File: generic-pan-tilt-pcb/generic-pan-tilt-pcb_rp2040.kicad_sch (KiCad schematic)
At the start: 28 parts, among them U1 RP2040, U2 W25Q32JVSS, Y1 ABM8-272-T3

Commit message: rename again to generic-pan-tilt
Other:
- title: Pan Tilt PCB: RP2040 -> Generic Pan Tilt PCB: RP2040

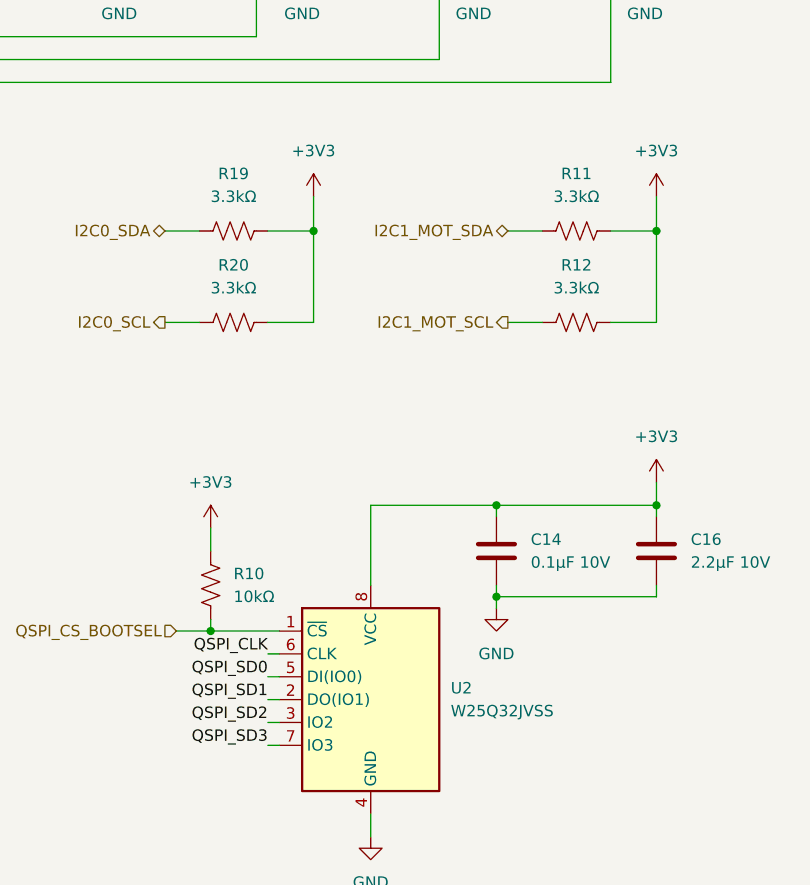
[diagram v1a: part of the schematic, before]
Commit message: pick all footprints, begin layout
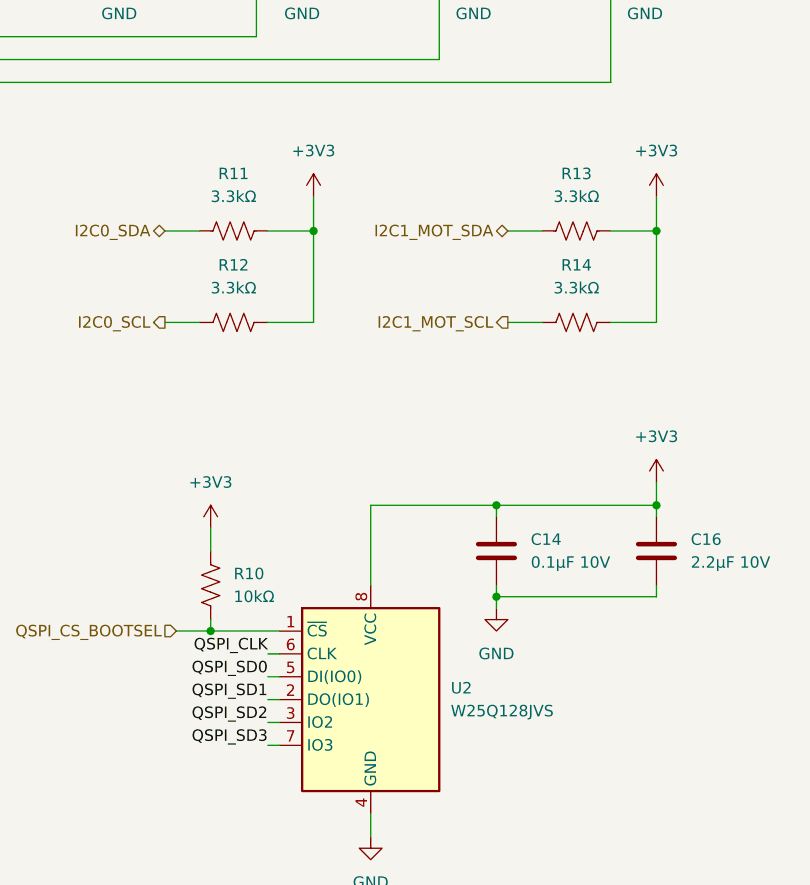
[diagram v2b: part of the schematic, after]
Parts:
- C1, C10, C11, C12, C13, C14, C15, C16, C2, C3, C4, C5, C6, C7, C8, C9: footprint (none) -> Capacitor_SMD:C_0603_1608Metric
- R10, R6, R7, R8, R9: footprint (none) -> Resistor_SMD:R_0603_1608Metric
- R11: renamed from R19; footprint (none) -> Resistor_SMD:R_0603_1608Metric
- R12: renamed from R20; footprint (none) -> Resistor_SMD:R_0603_1608Metric
- R13: renamed from R11; footprint (none) -> Resistor_SMD:R_0603_1608Metric
- R14: renamed from R12; footprint (none) -> Resistor_SMD:R_0603_1608Metric
- U2: value W25Q32JVSS -> W25Q128JVS; symbol Memory_Flash:W25Q32JVSS -> Memory_Flash:W25Q128JVS
- Y1: footprint (none) -> Crystal:Crystal_SMD_3225-4Pin_3.2x2.5mm

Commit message: layout progress
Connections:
- net USB_UNTERMINATED_D+: now reaches R7.2, U1.46 (USB_DM)
- net USB_UNTERMINATED_D-: now reaches R6.2, U1.47 (USB_DP)
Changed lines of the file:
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@@
+		)
+	)
+	(label "USB_UNTERMINATED_D+"
+		(at 43.18 86.36 0)
+		(fields_autoplaced yes)
+		(effects
+			(font
+				(size 1.27 1.27)
+			)
+			(justify left bottom)
 		)
 	)
@@
 		)
 	)
+	(label "USB_UNTERMINATED_D-"
+		(at 43.18 83.82 0)
+		(fields_autoplaced yes)
+		(effects
+			(font
+				(size 1.27 1.27)
+			)
+			(justify left bottom)
+		)
+	)

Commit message: begin new routing
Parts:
- C1, C10, C11, C12, C13, C14, C15, C16, C2, C3, C4, C5, C6, C7, C8, C9: footprint Capacitor_SMD:C_0603_1608Metric -> Capacitor_SMD:C_0402_1005Metric
- R10, R11, R12, R13, R14, R6, R7, R8, R9: footprint Resistor_SMD:R_0603_1608Metric -> Capacitor_SMD:C_0402_1005Metric
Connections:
- net XIN: now reaches C1.2, U1.20 (XIN), Y1.4
- net XOUT: now reaches R9.2, U1.21 (XOUT)
- net XOUT_R: now reaches C2.2, R9.1, Y1.2
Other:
- moved on the sheet: C1, C2, R9, Y1

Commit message: more pcb, kicost maf digikey mouser
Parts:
- U1: digikey# (none) -> 2648-SC0914(13)CT-ND; manf# (none) -> SC0914(13); mouser# (none) -> 358-SC091413
- U2: digikey# (none) -> W25Q128JVSIQCT-ND; manf# (none) -> W25Q128JVSIQ TR; mouser# (none) -> 454-W25Q128JVSIQTR
- Y1: digikey# (none) -> 535-ABM8-272-T3CT-ND; manf# (none) -> ABM8-272-T3; mouser# (none) -> 815-ABM8-272-T3
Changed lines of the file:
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@@
+			)
+		)
+		(property "manf#" "SC0914(13)"
+			(at 93.98 114.3 0)
+			(effects
+				(font
+					(size 1.27 1.27)
+				)
+				(hide yes)
+			)
+		)
+		(property "digikey#" "2648-SC0914(13)CT-ND"
+			(at 93.98 114.3 0)
+			(effects
+				(font
+					(size 1.27 1.27)
+				)
+				(hide yes)
+			)
+		)
+		(property "mouser#" "358-SC091413"
+			(at 93.98 114.3 0)
+			(effects
+				(font
+					(size 1.27 1.27)
+				)
+				(hide yes)
 			)
 		)
@@
 			)
 		)
+		(property "digikey#" "W25Q128JVSIQCT-ND"
+			(at 210.82 125.73 0)
+			(effects
+				(font
+					(size 1.27 1.27)
+				)
+				(hide yes)
+			)
+		)
+		(property "manf#" "W25Q128JVSIQ TR"
+			(at 210.82 125.73 0)
+			(effects
+				(font
+					(size 1.27 1.27)
+				)
+				(hide yes)
+			)
+		)
+		(property "mouser#" "454-W25Q128JVSIQTR"
+			(at 210.82 125.73 0)
+			(effects
+				(font
+					(size 1.27 1.27)
+				)
+				(hide yes)
+			)
+		)
 		(pin "8"
 		)
@@
 			(at 41.91 127 0)
 			(effects
+				(font
+					(size 1.27 1.27)
+				)
+				(hide yes)
+			)
+		)
+		(property "digikey#" "535-ABM8-272-T3CT-ND"
+			(at 41.91 127 0)
+			(effects
+				(font
+					(size 1.27 1.27)
+				)
+				(hide yes)
+			)
+		)
+		(property "manf#" "ABM8-272-T3"
+			(at 41.91 127 0)
+			(effects
+				(font
+					(size 1.27 1.27)
+				)
+				(hide yes)
+			)
+		)
+		(property "mouser#" "815-ABM8-272-T3"
+			(at 41.91 127 0)
+			(effects

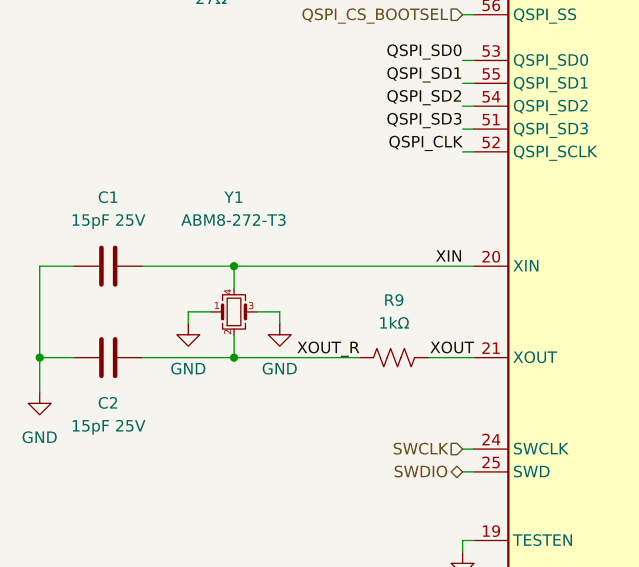
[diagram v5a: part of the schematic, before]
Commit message: transplant hardware guide rp2040
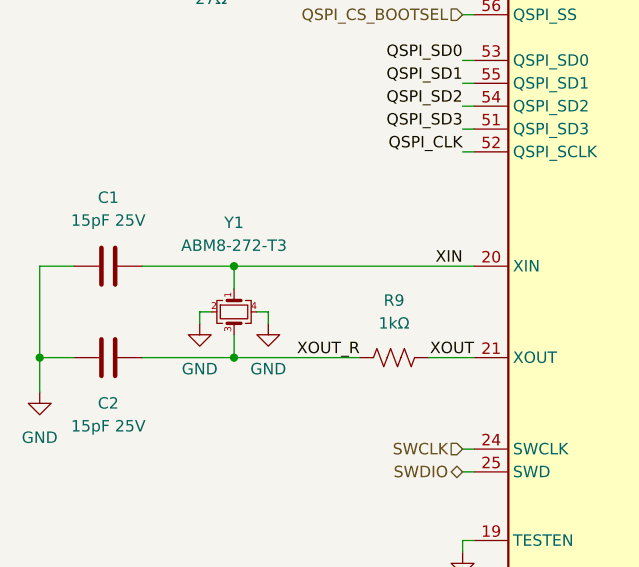
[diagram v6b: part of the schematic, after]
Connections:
- net GND: now also Y1.2, Y1.4; no longer Y1.1, Y1.3
- net XIN: now also Y1.1; no longer Y1.4
- net XOUT_R: now also Y1.3; no longer Y1.2
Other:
- moved on the sheet: Y1
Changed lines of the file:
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@@
 	(wire
 		(pts
-			(xy 36.83 127) (xy 39.37 127)
+			(xy 38.1 127) (xy 39.37 127)
 		)
 		(stroke
@@
 	(wire
 		(pts
+			(xy 44.45 127) (xy 45.72 127)
+		)
+		(stroke
+			(width 0)
+			(type default)
+		)
+	)
+	(wire
+		(pts
 			(xy 226.06 83.82) (xy 229.87 83.82)
 		)
@@
 	(wire
 		(pts
-			(xy 46.99 128.27) (xy 46.99 127)
+			(xy 45.72 128.27) (xy 45.72 127)
 		)
 		(stroke
@@
 	(wire
 		(pts
-			(xy 36.83 128.27) (xy 36.83 127)
+			(xy 38.1 128.27) (xy 38.1 127)
 		)
 		(stroke
@@
 		)
 	)
-	(wire
-		(pts
-			(xy 44.45 127) (xy 46.99 127)
-		)
-		(stroke
-			(width 0)
-			(type default)
-		)
-	)
 	(label "QSPI_SD0"
 		(at 199.39 123.19 180)
@@
 	(symbol
 		(lib_id "power:GND")
-		(at 46.99 128.27 0)
+		(at 45.72 128.27 0)
 		(unit 1)
 		(exclude_from_sim no)
@@
 		(fields_autoplaced yes)
 		(property "Reference" "#PWR024"
-			(at 46.99 134.62 0)
+			(at 45.72 134.62 0)
 			(effects
 				(font
@@
 		)
 		(property "Value" "GND"
-			(at 46.99 133.35 0)
+			(at 45.72 133.35 0)
 			(effects
 				(font
@@
 		)
 		(property "Footprint" ""
-			(at 46.99 128.27 0)
+			(at 45.72 128.27 0)
 			(effects
 				(font
@@
 		)
 		(property "Datasheet" ""
-			(at 46.99 128.27 0)
+			(at 45.72 128.27 0)
 			(effects
 				(font
@@
 		)
 		(property "Description" "Power symbol creates a global label with name \"GND\" , ground"
-			(at 46.99 128.27 0)
+			(at 45.72 128.27 0)
 			(effects
 				(font
@@
 	(symbol
 		(lib_id "Device:Crystal_GND24_Small")
-		(at 41.91 127 0)
+		(at 41.91 127 270)
 		(unit 1)
 		(exclude_from_sim no)
@@
 		(dnp no)
 		(property "Reference" "Y1"
-			(at 41.91 114.3 0)
+			(at 41.91 117.094 90)
 			(effects
 				(font
@@
 		)
 		(property "Value" "ABM8-272-T3"
-			(at 41.91 116.84 0)
+			(at 41.91 119.634 90)
 			(effects
 				(font
@@
 	(symbol
 		(lib_id "power:GND")
-		(at 36.83 128.27 0)
+		(at 38.1 128.27 0)
 		(unit 1)
 		(exclude_from_sim no)
@@
 		(fields_autoplaced yes)
 		(property "Reference" "#PWR021"
-			(at 36.83 134.62 0)
+			(at 38.1 134.62 0)
 			(effects
 				(font
@@
 		)
 		(property "Value" "GND"
-			(at 36.83 133.35 0)
+			(at 38.1 133.35 0)
 			(effects
 				(font
@@
 		)
 		(property "Footprint" ""
-			(at 36.83 128.27 0)
+			(at 38.1 128.27 0)
 			(effects
 				(font
@@
 		)
 		(property "Datasheet" ""
-			(at 36.83 128.27 0)
+			(at 38.1 128.27 0)
 			(effects
 				(font
@@
 		)
 		(property "Description" "Power symbol creates a global label with name \"GND\" , ground"
-			(at 36.83 128.27 0)
+			(at 38.1 128.27 0)
 			(effects
 				(font

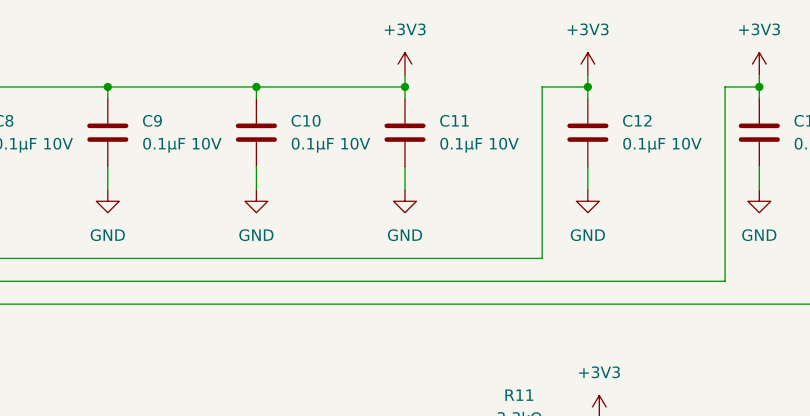
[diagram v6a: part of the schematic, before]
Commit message: mostly done with rp2040, horizontal usb
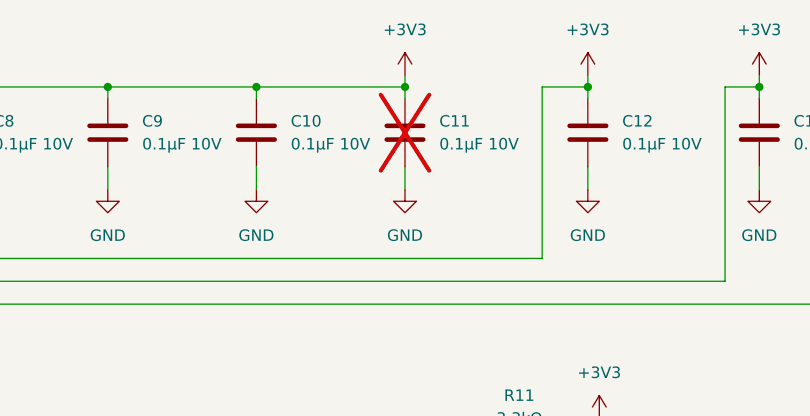
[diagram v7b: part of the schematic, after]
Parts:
- C11: now not fitted; now left out of the parts list
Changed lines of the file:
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@@
 		(unit 1)
 		(exclude_from_sim no)
-		(in_bom yes)
-		(on_board yes)
-		(dnp no)
+		(in_bom no)
+		(on_board no)
+		(dnp yes)
 		(fields_autoplaced yes)
 		(property "Reference" "C11"
